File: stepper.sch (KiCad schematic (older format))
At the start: 84 parts, among them IC1 PC817, IC2 PC817, IC3 PC817, IC4 PC817, IC5 PC817, IC6 PC817, P1 CONN_2, P2 CONN_8, P3 CONN_4, P4 CONN_4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

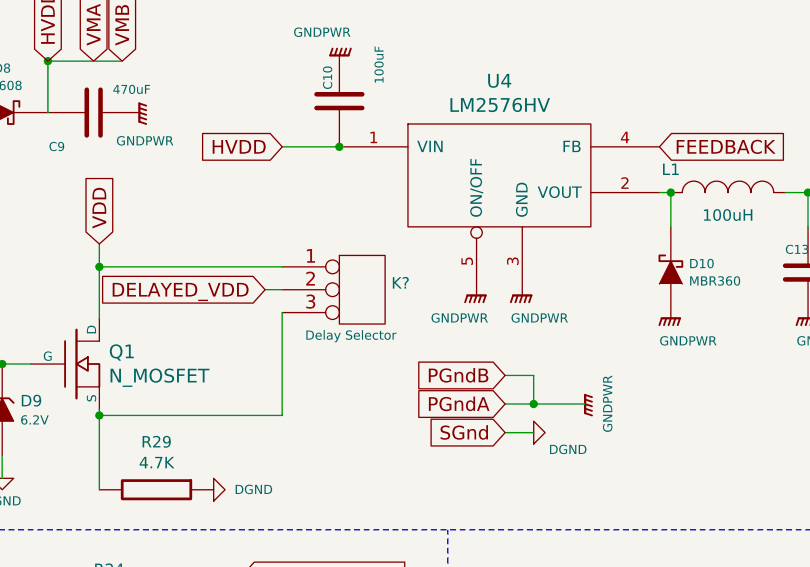
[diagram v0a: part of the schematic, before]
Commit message: adjust board, change lm2576 package
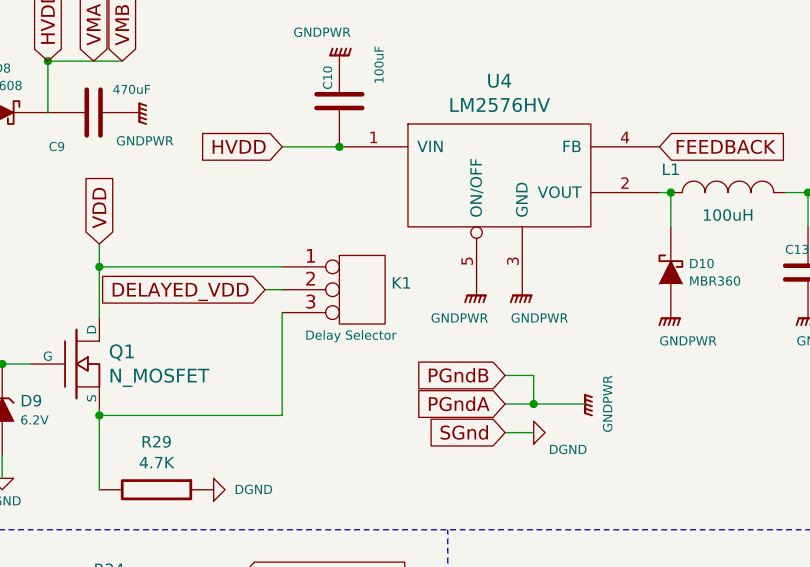
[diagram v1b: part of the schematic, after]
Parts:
- K1: renamed from K?; footprint (none) -> Pin_Headers:Pin_Header_Straight_1x03
- U4: footprint I20:TO-263-5 -> TO_SOT_Packages_THT:Pentawatt_Neutral_Staggered_Verical_TO220-5-T05D
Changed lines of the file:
@@
 F 0 "U4" H 7200 1687 60  0000 C CNN
 F 1 "LM2576HV" H 7200 1581 60  0000 C CNN
-F 2 "I20:TO-263-5" H 7200 1300 60  0001 C CNN
+F 2 "TO_SOT_Packages_THT:Pentawatt_Neutral_Staggered_Verical_TO220-5-T05D" H 7200 1300 60  0001 C CNN
 F 3 "" H 7200 1300 60  0001 C CNN
 F 4 "Texas Instruments" H 7200 1650 60  0001 C CNN "Manufacturer"
@@
 Connection ~ 5025 2150
 $Comp
-L CONN_3 K?
+L CONN_3 K1
 U 1 1 5821D1C2
 P 6600 1825
-F 0 "K?" H 6727 1853 50  0000 L CNN
+F 0 "K1" H 6727 1853 50  0000 L CNN
 F 1 "Delay Selector" H 6350 1625 40  0000 L CNN
-F 2 "" H 6600 1825 60  0001 C CNN
+F 2 "Pin_Headers:Pin_Header_Straight_1x03" H 6600 1825 60  0001 C CNN
 F 3 "" H 6600 1825 60  0001 C CNN
 	1    6600 1825

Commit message: add screenshot
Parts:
- U4: footprint TO_SOT_Packages_THT:Pentawatt_Neutral_Staggered_Verical_TO220-5-T05D -> I20:Pentawatt_Neutral_Staggered_Verical_TO220-5-T05D
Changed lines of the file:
@@
 F 0 "U4" H 7200 1687 60  0000 C CNN
 F 1 "LM2576HV" H 7200 1581 60  0000 C CNN
-F 2 "TO_SOT_Packages_THT:Pentawatt_Neutral_Staggered_Verical_TO220-5-T05D" H 7200 1300 60  0001 C CNN
+F 2 "I20:Pentawatt_Neutral_Staggered_Verical_TO220-5-T05D" H 7200 1300 60  0001 C CNN
 F 3 "" H 7200 1300 60  0001 C CNN
 F 4 "Texas Instruments" H 7200 1650 60  0001 C CNN "Manufacturer"
